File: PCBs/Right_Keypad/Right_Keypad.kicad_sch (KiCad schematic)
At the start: 57 parts, among them J1 Conn_Right_Keypad, SW1 SW_Push, SW10 SW_Push, SW11 SW_Push, SW12 SW_Push, SW13 SW_Push, SW14 SW_Push, SW15 SW_Push, SW16 SW_Push, SW17 SW_Push, SW18 SW_Push, SW19 SW_Push, SW2 SW_Push, SW20 SW_Push, SW21 SW_Push, SW22 SW_Push, SW23 SW_Push, SW24 SW_Push, SW3 SW_Push, SW4 SW_Push, SW5 SW_Push, SW6 SW_Push, SW7 SW_Push, SW8 SW_Push, SW9 SW_Push, U1 74HC165

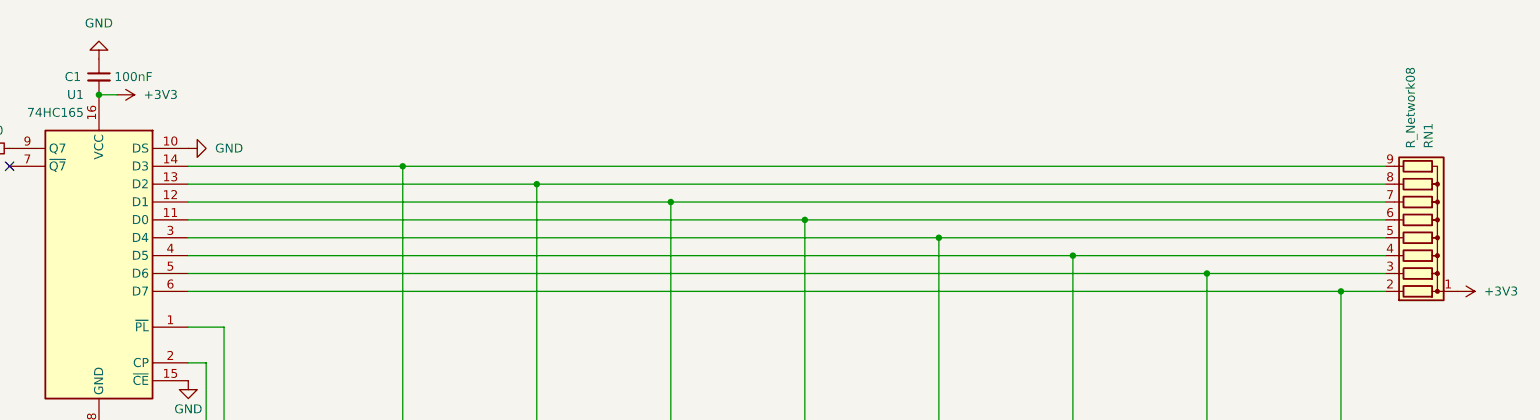
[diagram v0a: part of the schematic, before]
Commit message: Fix 74HC4051 enable, set pull-up values, name keypad column nets
Shared_Main:
- U2 (74HC4051) pin 6 (~E) was tied to +3V3, permanently inhibiting all
  eight analog channels. Moved to GND. The pad had no tracks on it, so
  the board change is just which plane claims it (In2 +3V3 -> In1 GND);
  all zones refilled.
- RN1-RN6 pull-up arrays had no value assigned (still reading the
  R_Network08 symbol default). Set to 10k, matching RN8. Board footprint
  value fields synced to match.
- Also includes graphical tidy-up of junction/wire placement (no netlist
  change).

Right_Keypad:
- RN1 pull-up array set to 10k, board field synced.
- U1 was using a locally modified 74HC165 whose D0-D3 pins had been moved
  (via Swap Pins) so the column rails fan out to RN1 without crossing.
  That recorded the bit-order decision in pin geometry, where nothing
  diffs it and an "Update Symbols from Library" would silently remap four
  nets. Reverted U1 to the stock 74xx:74HC165 and expressed the same
  mapping as named nets COL1-COL8 instead:

      COL1 -> D3   COL5 -> D4
      COL2 -> D2   COL6 -> D5
      COL3 -> D1   COL7 -> D6
      COL4 -> D0   COL8 -> D7

  Connectivity is unchanged - verified by diffing before/after netlists
  with net names stripped and each net's pin set sorted. No copper moved
  (363 segments, 8 vias, 57 footprints before and after); only net names
  changed on the board.

Both projects: ERC 0, DRC 0, 0 unconnected, 0 schematic parity issues.

Co-Authored-By: Claude Opus 5 <noreply@anthropic.com>
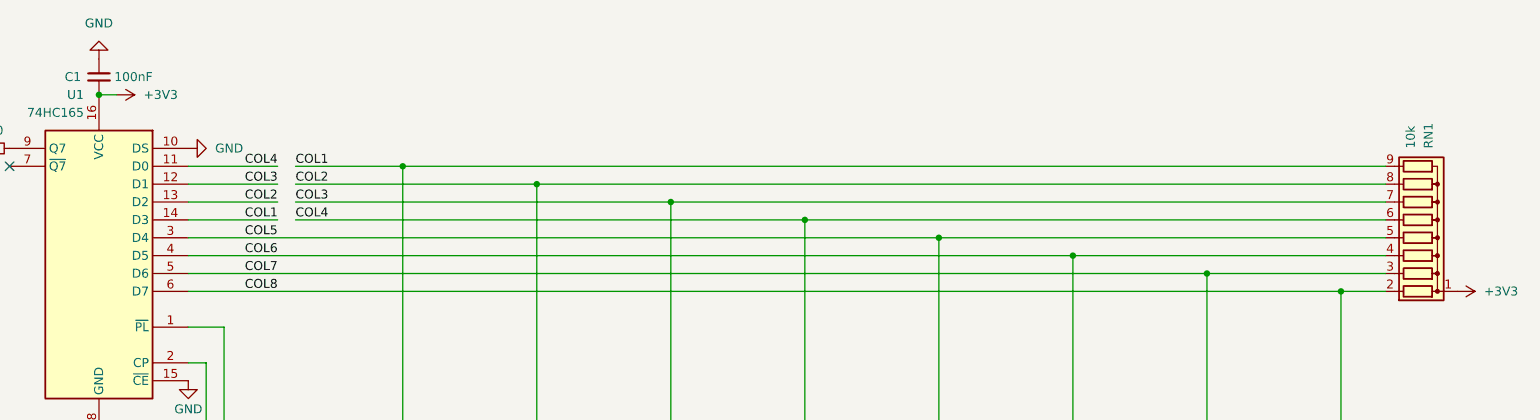
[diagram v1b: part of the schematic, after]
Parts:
- RN1: value R_Network08 -> 10k
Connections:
- net COL4: now reaches D12.2 (A), D20.2 (A), D4.2 (A), RN1.6 (R5), U1.11 (D0)
- net COL3: now reaches D11.2 (A), D19.2 (A), D3.2 (A), RN1.7 (R6), U1.12 (D1)
- net COL2: now reaches D10.2 (A), D18.2 (A), D2.2 (A), RN1.8 (R7), U1.13 (D2)
- net COL1: now reaches D1.2 (A), D17.2 (A), D9.2 (A), RN1.9 (R8), U1.14 (D3)
- net COL5: now reaches D13.2 (A), D21.2 (A), D5.2 (A), RN1.5 (R4), U1.3 (D4)
- net COL6: now reaches D14.2 (A), D22.2 (A), D6.2 (A), RN1.4 (R3), U1.4 (D5)
- net COL7: now reaches D15.2 (A), D23.2 (A), D7.2 (A), RN1.3 (R2), U1.5 (D6)
- net COL8: now reaches D16.2 (A), D24.2 (A), D8.2 (A), RN1.2 (R1), U1.6 (D7)
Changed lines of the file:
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@@
 	(wire
 		(pts
+			(xy 91.44 50.8) (xy 104.14 50.8)
+		)
+		(stroke
+			(width 0)
+			(type default)
+		)
+	)
+	(wire
+		(pts
 			(xy 255.27 111.76) (xy 255.27 129.54)
 		)
@@
 	(wire
 		(pts
-			(xy 91.44 53.34) (xy 140.97 53.34)
+			(xy 106.68 53.34) (xy 140.97 53.34)
 		)
 		(stroke
@@
 	(wire
 		(pts
+			(xy 91.44 53.34) (xy 104.14 53.34)
+		)
+		(stroke
+			(width 0)
+			(type default)
+		)
+	)
+	(wire
+		(pts
 			(xy 123.19 121.92) (xy 142.24 121.92)
 		)
@@
 	(wire
 		(pts
-			(xy 91.44 58.42) (xy 179.07 58.42)
+			(xy 106.68 58.42) (xy 179.07 58.42)
 		)
 		(stroke
@@
 	(wire
 		(pts
-			(xy 91.44 50.8) (xy 121.92 50.8)
+			(xy 106.68 50.8) (xy 121.92 50.8)
 		)
 		(stroke
@@
 	(wire
 		(pts
+			(xy 91.44 55.88) (xy 104.14 55.88)
+		)
+		(stroke
+			(width 0)
+			(type default)
+		)
+	)
+	(wire
+		(pts
 			(xy 21.59 99.06) (xy 21.59 101.6)
 		)
@@
 	(wire
 		(pts
+			(xy 91.44 58.42) (xy 104.14 58.42)
+		)
+		(stroke
+			(width 0)
+			(type default)
+		)
+	)
+	(wire
+		(pts
 			(xy 179.07 111.76) (xy 179.07 129.54)
 		)
@@
 	(wire
 		(pts
-			(xy 91.44 55.88) (xy 160.02 55.88)
+			(xy 106.68 55.88) (xy 160.02 55.88)
 		)
 		(stroke
@@
 		)
 	)
+	(label "COL8"
+		(at 104.14 68.58 180)
+		(effects
+			(font
+				(size 1.27 1.27)
+			)
+			(justify right bottom)
+		)
+	)
+	(label "COL3"
+		(at 104.14 53.34 180)
+		(effects
+			(font
+				(size 1.27 1.27)
+			)
+			(justify right bottom)
+		)
+	)
+	(label "COL2"
+		(at 106.68 53.34 0)
+		(effects
+			(font
+				(size 1.27 1.27)
+			)
+			(justify left bottom)
+		)
+	)
+	(label "COL1"
+		(at 104.14 58.42 180)
+		(effects
+			(font
+				(size 1.27 1.27)
+			)
+			(justify right bottom)
+		)
+	)
+	(label "COL5"
+		(at 104.14 60.96 180)
+		(effects
+			(font
+				(size 1.27 1.27)
+			)
+			(justify right bottom)
+		)
+	)
+	(label "COL6"
+		(at 104.14 63.5 180)
+		(effects
+			(font
+				(size 1.27 1.27)
+			)
+			(justify right bottom)
+		)
+	)
+	(label "COL4"
+		(at 106.68 58.42 0)
+		(effects
+			(font
+				(size 1.27 1.27)
+			)
+			(justify left bottom)
+		)
+	)
+	(label "COL2"
+		(at 104.14 55.88 180)
+		(effects
+			(font
+				(size 1.27 1.27)
+			)
+			(justify right bottom)
+		)
+	)
+	(label "COL4"
+		(at 104.14 50.8 180)
+		(effects
+			(font
+				(size 1.27 1.27)
+			)
+			(justify right bottom)
+		)
+	)
+	(label "COL3"
+		(at 106.68 55.88 0)
+		(effects
+			(font
+				(size 1.27 1.27)
+			)
+			(justify left bottom)
+		)
+	)
+	(label "COL7"
+		(at 104.14 66.04 180)
+		(effects
+			(font
+				(size 1.27 1.27)
+			)
+			(justify right bottom)
+		)
+	)
+	(label "COL1"
+		(at 106.68 50.8 0)
+		(effects
+			(font
+				(size 1.27 1.27)
+			)
+			(justify left bottom)
+		)
+	)
 	(symbol
 		(lib_id "Switch:SW_Push")
@@
 			)
 		)
-		(property "Value" "R_Network08"
+		(property "Value" "10k"
 			(at 265.1761 48.26 0)
 			(show_name no)
